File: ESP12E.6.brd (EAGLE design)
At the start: 36.6 x 36.6 mm, 50 parts, among them CN2 1X4-BIG, J1 1X2-3.5MM, J4 1X2-3.5MM, U1 A5984-TSSOP, U2 SPX3819M5-L-3-3

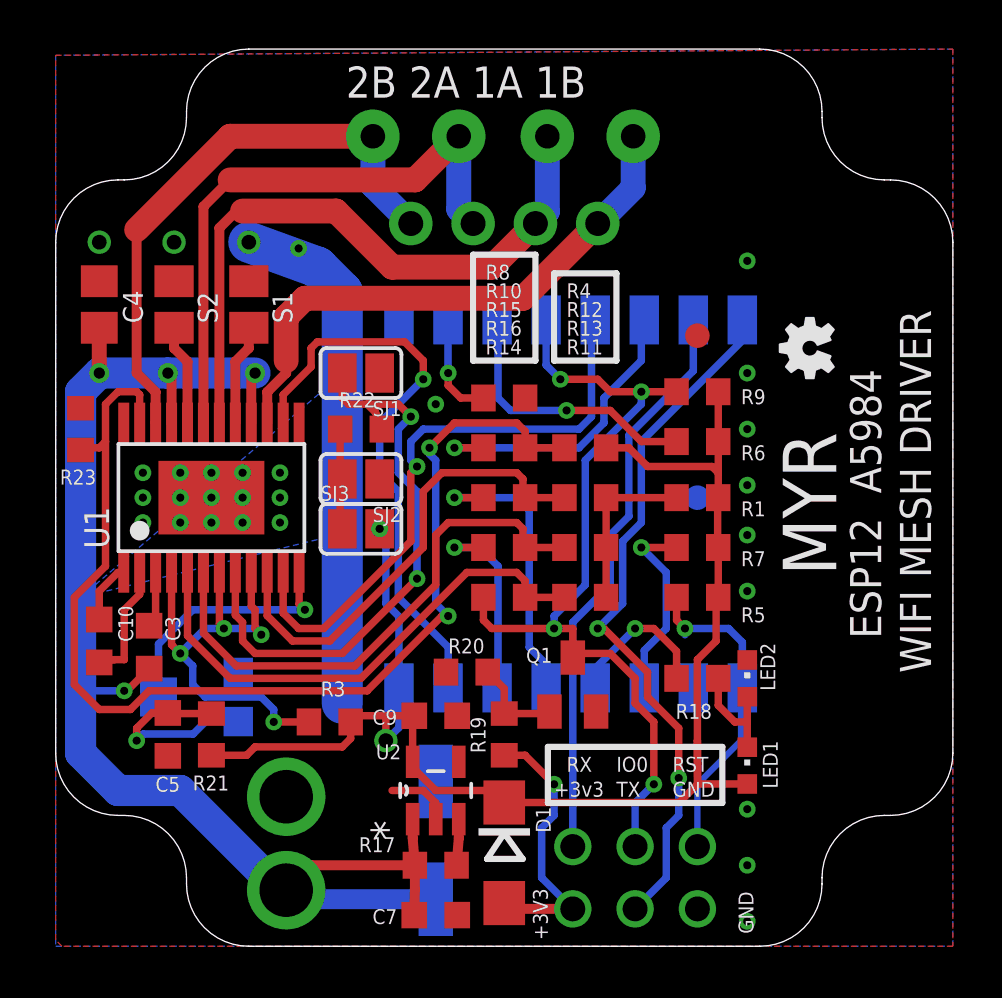
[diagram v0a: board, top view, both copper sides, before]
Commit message: GPIO pins repurposed
GPIO 12 and 14 broken out to to pin headers for general use. Required
that the MS section of board to be modified. GPIO0 now can control step
mode between 0 and 32 micro-stepping.
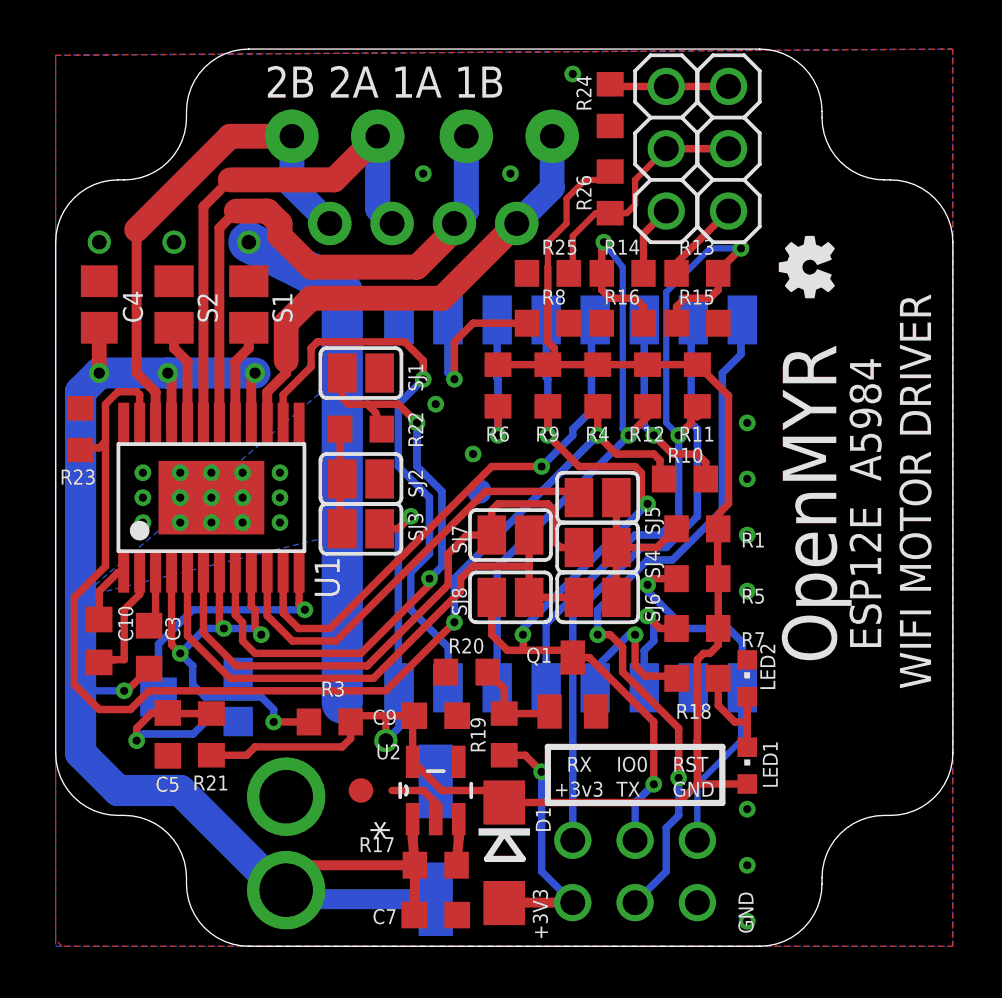
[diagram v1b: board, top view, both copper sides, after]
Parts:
- added JP7, JP8: (no value), adafruit:1X03
- added R24, R25, R26: DNP, adafruit:R0603
- added SJ4, SJ5, SJ6, SJ7, SJ8: (no value), jumper:SJ
- R13: value DNP -> 0
- R14: value 10k -> 0
- R15, R16: value 10k -> DNP
- U1: value A5984-TSSOP -> A5984
- moved FD2 23.1 mm to (12.4, 6.35)
- moved R14 14.1 mm to (23.1, 27.4), turned to 0 degrees
- moved R13 12.1 mm to (26.2, 27.4)
- moved R15 10.6 mm to (26.2, 25.4)
- moved R16 10.3 mm to (23.1, 25.4), turned to 0 degrees
- moved R11 9.77 mm to (26.2, 22.9), turned to 270 degrees
- moved FD1 8.89 mm to (17.3, 18.5)
- moved R6 8.44 mm to (18.0, 22.9), turned to 90 degrees
- moved R10 7.47 mm to (25.7, 19.1), turned to 0 degrees
- moved R9 6.10 mm to (20.1, 22.9), turned to 90 degrees
- moved R12 5.23 mm to (24.1, 22.9), turned to 270 degrees
- moved R8 3.53 mm to (20.1, 25.4)
- moved CN2 3.30 mm to (18.8, 29.5)
- moved J1 3.30 mm to (11.4, 33.0)
- moved J4 3.30 mm to (18.5, 33.0)
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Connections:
- new net N$10: JP7.2, JP8.2, R25.1, R26.2
- new net N$12: JP8.1, R14.2
- new net N$3: JP7.1, R13.2
- new net N$9: JP7.3, JP8.3, R24.2
- net +3V3: now also R11.1, R12.1, R26.1
- net GND: now also R15.1, R16.1, R24.1, R25.2
- net GPIO0: now also SJ8.1; no longer R14.2
- net GPIO12: now also R12.2, R14.1
- net GPIO14: now also R11.2, R13.1
- net MSN: now also SJ4.2, SJ5.2, SJ6.2; no longer R11.1, R12.1, R13.1
- net XMS1: now also SJ6.1, SJ7.1, SJ8.2; no longer R11.2, R14.1
- net XMS2: now also SJ4.1, SJ7.2; no longer R13.2, R16.1
- net XMS3: now also SJ5.1; no longer R12.2, R15.1
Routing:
- net GPIO12: track 8.25 -> 26.9 mm, vias 1 -> 2
- net GPIO14: track 12.0 -> 29.3 mm, vias 1 -> 2
- net +3V3: track 59.5 -> 75.7 mm
- net N$10: track 0.00 -> 10.0 mm
- net GPIO2: track 11.2 -> 5.90 mm
- net N$9: track 0.00 -> 4.97 mm
- net GPIO4: track 12.6 -> 8.12 mm
- net 1B: track 23.1 -> 19.6 mm
- net N$3: track 0.00 -> 3.42 mm
- net CH_PD: track 7.95 -> 4.59 mm
- net 2B: track 23.6 -> 20.3 mm
- net 2A: track 24.2 -> 20.9 mm
- net GPIO15: track 4.32 -> 7.33 mm
- net N$12: track 0.00 -> 2.92 mm
- net 1A: track 26.6 -> 23.7 mm
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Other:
- board text added: "ESP12E A5984"
- board text added: "IO12"
- board text added: "IO14"
- board text added: "OpenMYR"
- board text added: "WIFI MOTOR DRIVER"
- board text removed: "ESP12 A5984"
- board text removed: "WIFI MESH DRIVER"

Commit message: Buck Regulator
Prototype +3.3V DC buck regultaor. Based around TI TPS62177 IC.
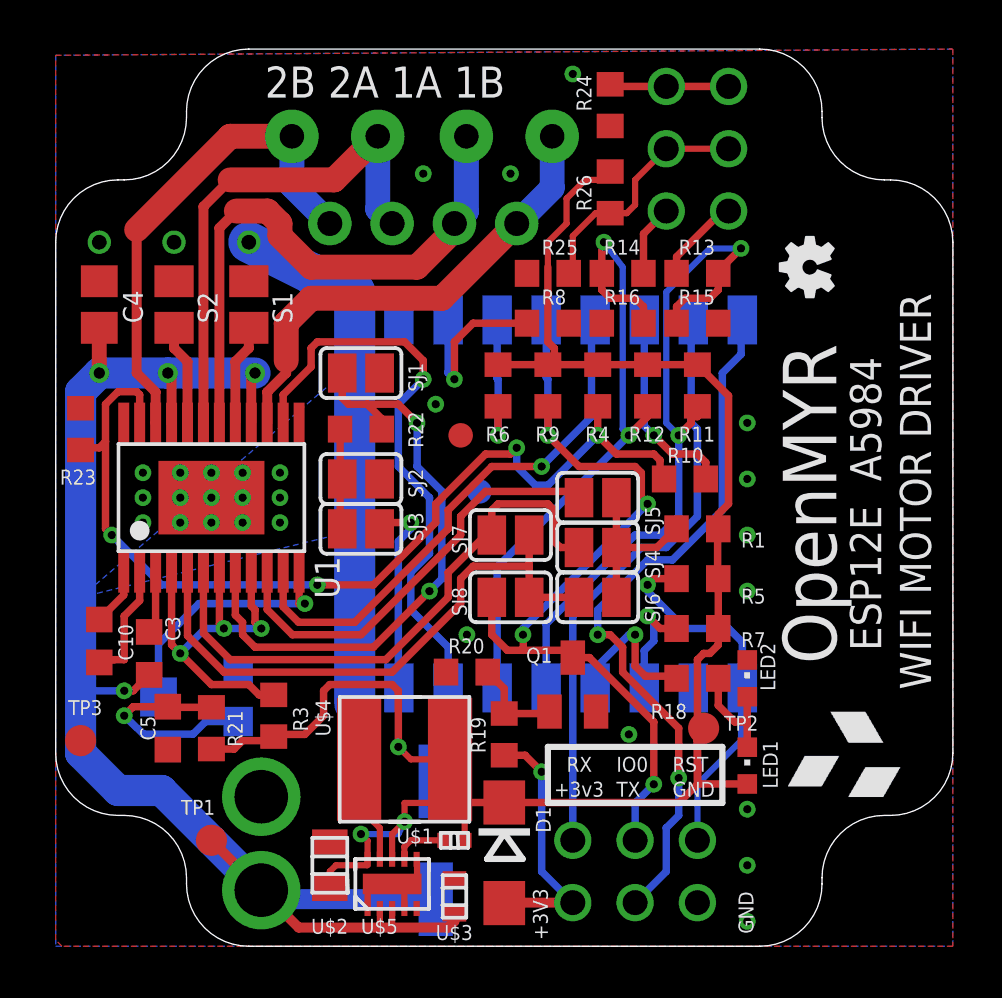
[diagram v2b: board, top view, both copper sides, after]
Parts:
- removed C7, C9: 10uF, adafruit:C0603K
- removed R17: 10k, adafruit:R0603
- removed U2: SPX3819M5-L-3-3, SPX3819M5-L-3-3:SOT95P280X145-5N
- added TP1, TP2, TP3: PTR1B1,27, testpad:B1,27
- added U$1: CRCW0402100KFKED, TPS62177:0402
- added U$2: GRM21BR60J226ME39L, TPS62177:0805
- added U$3: GRM188R61C225KE15D, TPS62177:0603
- added U$4: SDR0503-100ML, TPS62177:SDR0503
- added U$5: TPS62177DQCR, TPS62177:R-PWSON-N10
- moved FD2 15.0 mm to (16.5, 20.8)
- moved R3 2.30 mm to (8.89, 9.40), turned to 90 degrees
- moved C5 0.25 mm to (4.57, 8.89)
- moved R21 0.25 mm to (6.35, 8.89)
- moved C3 0.25 mm to (3.81, 11.9)
- flipped JP7 to the bottom
- flipped JP8 to the bottom
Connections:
- removed net N$4: R17.1, U2.3
- new net N$14: U$1.1, U$5.7
- new net N$17: U$4.1, U$5.9
- net +3V3: now also TP2.TP, U$1.2, U$2.2, U$4.2, U$5.10, U$5.8; no longer C9.1, U2.5
- net GND: now also TP3.TP, U$2.1, U$3.1, U$5.1, U$5.11, U$5.4, U$5.5, U$5.6; no longer C7.2, C9.2, U2.2
- net VMOT: now also TP1.TP, U$3.2, U$5.2, U$5.3; no longer C7.1, R17.2, U2.1
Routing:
- net +3V3: track 75.7 -> 89.3 mm, vias 2 -> 4
- net XENABLE: track 48.7 -> 40.1 mm, vias 2 -> 4
- net N$17: track 0.00 -> 5.77 mm
- net VMOT: track 58.5 -> 62.3 mm
- net XRESET: track 19.6 -> 16.6 mm, vias 4 -> 3
- net GND: track 23.9 -> 26.7 mm, vias 31 -> 32
- net N$14: track 0.00 -> 2.51 mm
- net N$4: track 1.88 -> 0.00 mm
- net N$1: track 8.29 -> 8.88 mm

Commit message: License Update
Licensed under CERN OHL v.1.2 or later
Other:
- board text added: "Project located at: https://github.com/OpenMYR/ESP12E.6/ Copyright Christopher Adams 2016. Licensed under CERN OHL v.1.2 or later This documentation is distributed WITHOUT ANY EXPRESS OR IMPLIED WARRANTY, INCLUDING OF MERCHANTABILITY, SATISFACTORY QUALITY AND FITNESS FOR A PARTICULAR PURPOSE. Please see the CERN OHL v.1.2 for applicable conditions"
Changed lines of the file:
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@@
 <rectangle x1="29.845" y1="6.5532" x2="29.9466" y2="6.5786" layer="21" rot="R90"/>
 <rectangle x1="29.845" y1="6.5278" x2="29.8958" y2="6.5532" layer="21" rot="R90"/>
+<text x="45.72" y="-0.254" size="1.778" layer="48">Project located at:
+https://github.com/OpenMYR/ESP12E.6/
+Copyright Christopher Adams 2016.
+Licensed under CERN OHL v.1.2 or later
+This documentation is distributed WITHOUT
+ANY EXPRESS OR IMPLIED WARRANTY,
+INCLUDING OF MERCHANTABILITY,
+SATISFACTORY QUALITY AND FITNESS
+FOR A PARTICULAR PURPOSE.
+Please see the CERN OHL v.1.2 for applicable conditions</text>
 </plain>
 <attributes>
@@
 </board>
 </drawing>
+<compatibility>
+<note version="6.3" minversion="6.2.2" severity="warning">
+Since Version 6.2.2 text objects can contain more than one line,
+which will not be processed correctly with this version.
+</note>
+</compatibility>
 </eagle>

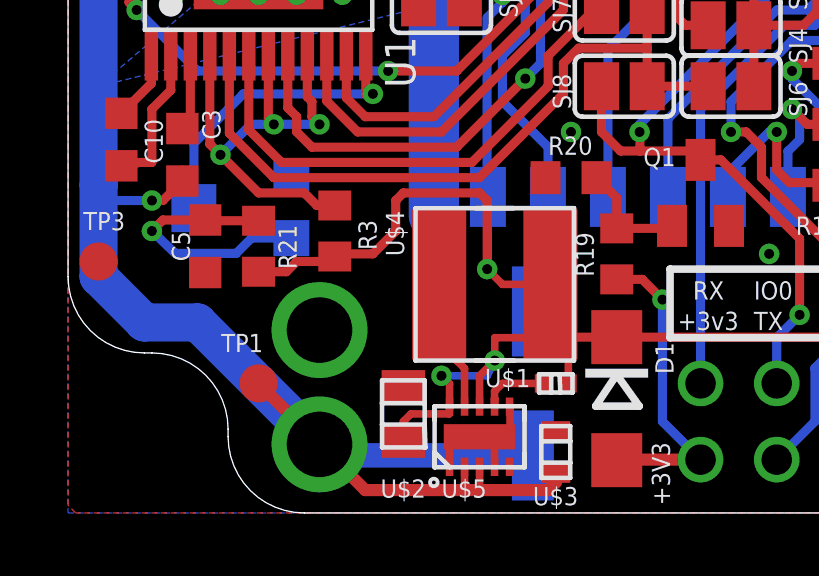
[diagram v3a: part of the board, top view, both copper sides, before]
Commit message: Power Isolation
Separation between VMOT/+3V3 and +3V3/GND nets is increased. Rearranged
R3,R21, U$3 and, U$2.
Removed U$1 in the regulator schematic as it was not nessesary.
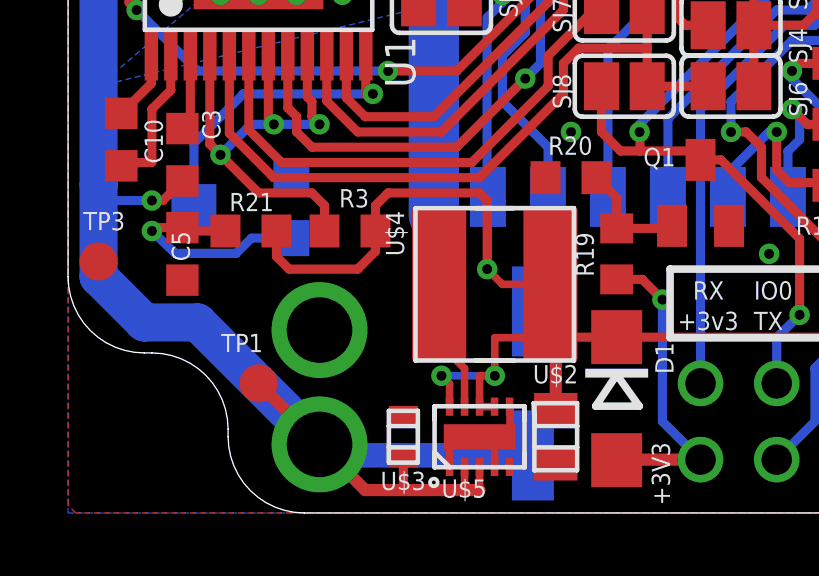
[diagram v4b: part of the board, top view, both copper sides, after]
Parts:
- removed U$1: CRCW0402100KFKED, TPS62177:0402
- moved U$2 5.14 mm to (16.3, 2.54), turned to 90 degrees
- moved U$3 5.11 mm to (11.2, 2.54)
- moved C5 0.80 mm to (3.81, 8.64)
- moved R21 0.57 mm to (6.10, 9.40), turned to 0 degrees
- moved R3 0.51 mm to (9.40, 9.40), turned to 180 degrees
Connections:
- removed net N$14: U$1.1, U$5.7
- net +3V3: now also U$5.7; no longer U$1.2
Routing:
- net N$14: track 2.51 -> 0.00 mm
- net VMOT: track 62.3 -> 60.4 mm
- net N$1: track 8.88 -> 7.70 mm
- net XRESET: track 16.6 -> 17.1 mm

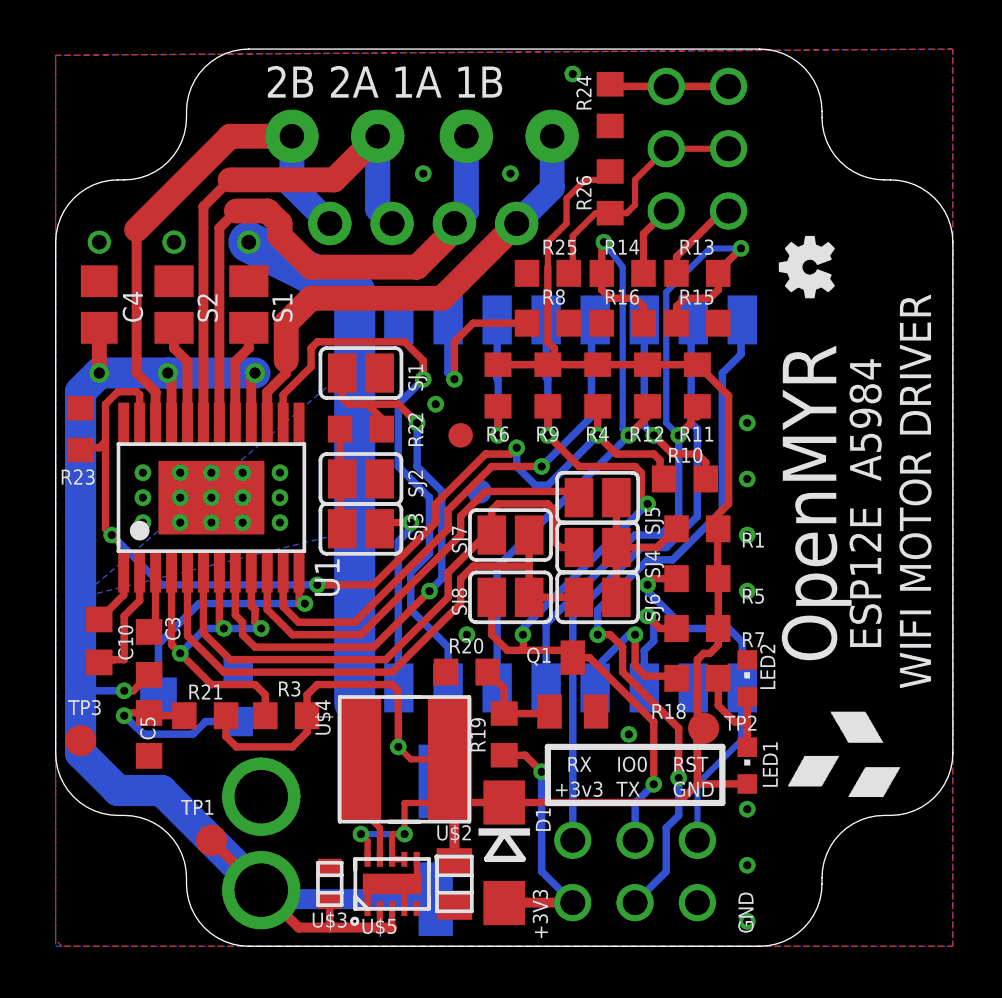
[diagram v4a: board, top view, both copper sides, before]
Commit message: //Lowered power via hole sizes to 18 AWG // Added ADC pin exposure
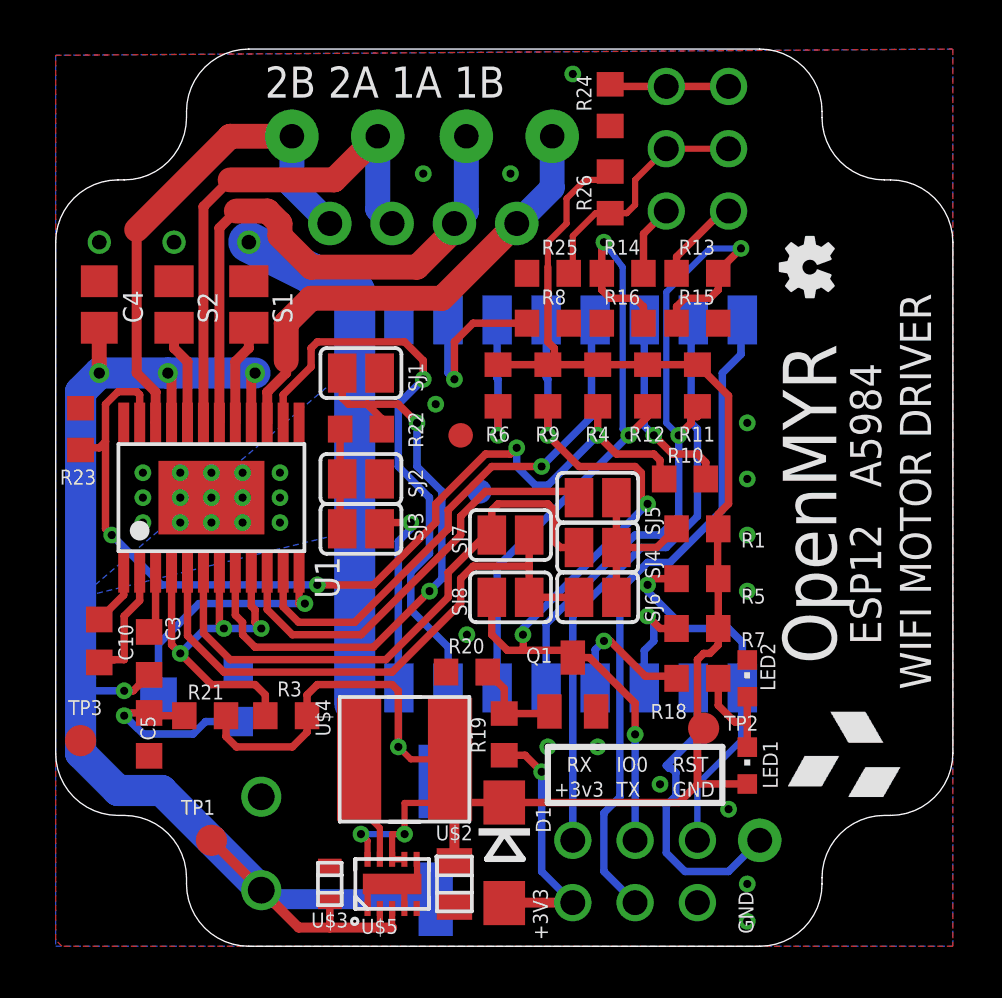
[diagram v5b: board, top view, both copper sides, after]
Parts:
- added JP3: (no value), adafruit:1X01-CLEANBIG
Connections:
- net ADC: now also JP3.1
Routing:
- net ADC: track 0.00 -> 12.4 mm
- net TXD: track 29.3 -> 27.2 mm, vias 2 -> 0
- net GPIO0: track 35.2 -> 34.6 mm
- net GPIO16: track 6.42 -> 5.92 mm
- net GND: vias 32 -> 34
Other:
- board text added: "ESP12 A5984"
- board text removed: "ESP12E A5984"
- board text removed: "MYR"

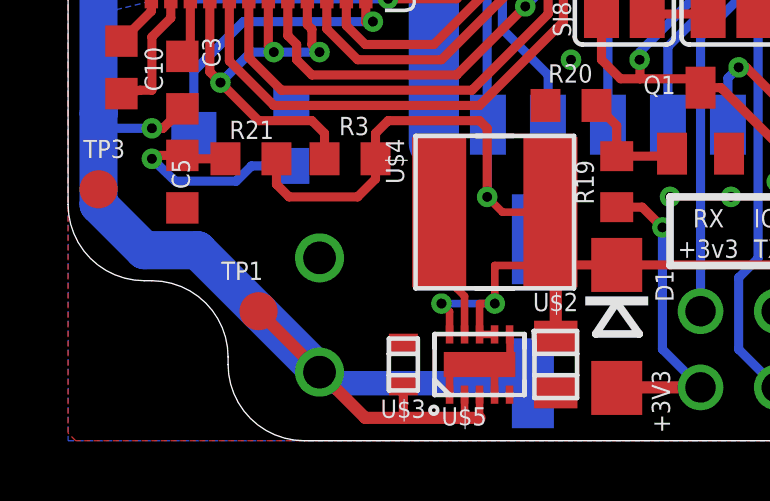
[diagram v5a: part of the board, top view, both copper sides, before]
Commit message: Oct Update
Power drill size change and placment of IO pin resistors
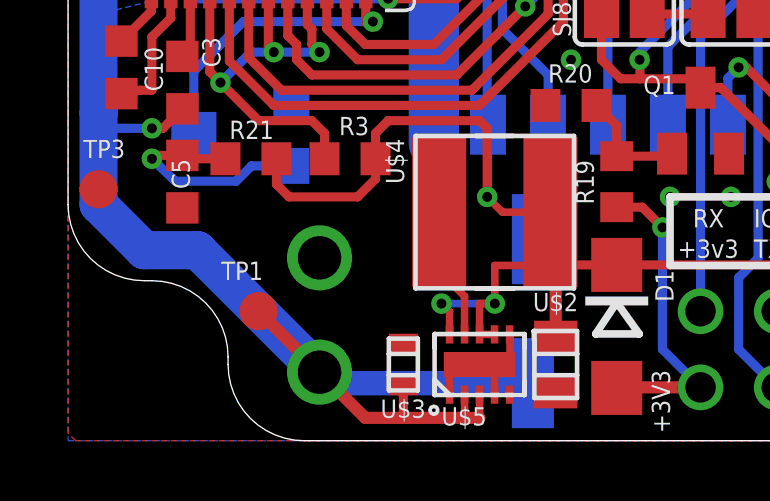
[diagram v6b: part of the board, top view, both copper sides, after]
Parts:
- R24, R26: value DNP -> 0
